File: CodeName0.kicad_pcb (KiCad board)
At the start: 4 copper layers, 60 x 80 mm, 96 parts, among them J1 STM32 Debug Conn, J2 Power Conn, J3 USB C 16p, J4 Telemetry Conn, J5 MicroSD, J6 GPS Conn, J7 Buzzer Conn, J8 ESP32 Jumper Conn, J9 ESP32 Programming Conn, Q1 MMBT3904, SW1 Tactile Switch, SW2 Tactile Switch, SW3 Tactile Switch, SW4 Tactile Switch, U1 TPS5430DDAR, U2 LDO, U3 STM32H743VITx, U4 ICM-42688-P, U5 BMP388, U6 ESP32 C3 WROOM 02U, Y1 Crystal_GND24

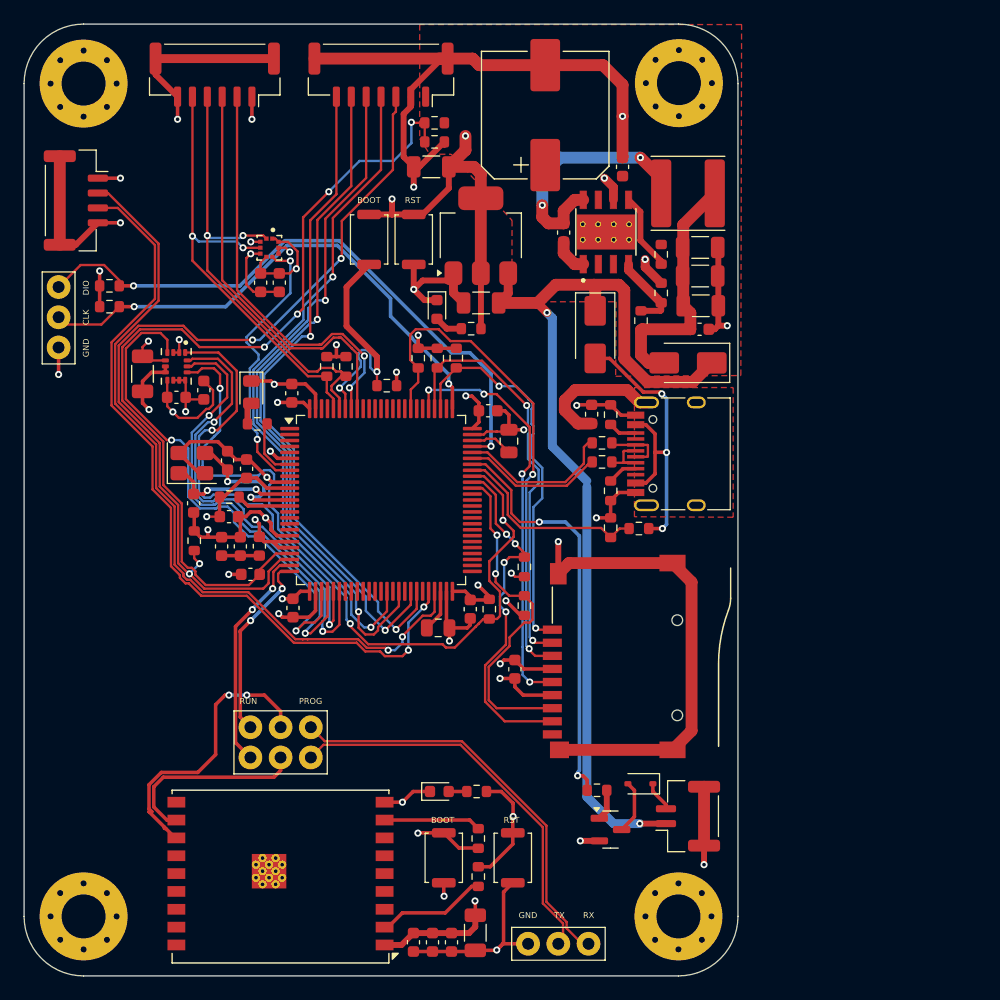
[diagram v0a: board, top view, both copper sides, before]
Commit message: feat: remove esp32-c3 wroom
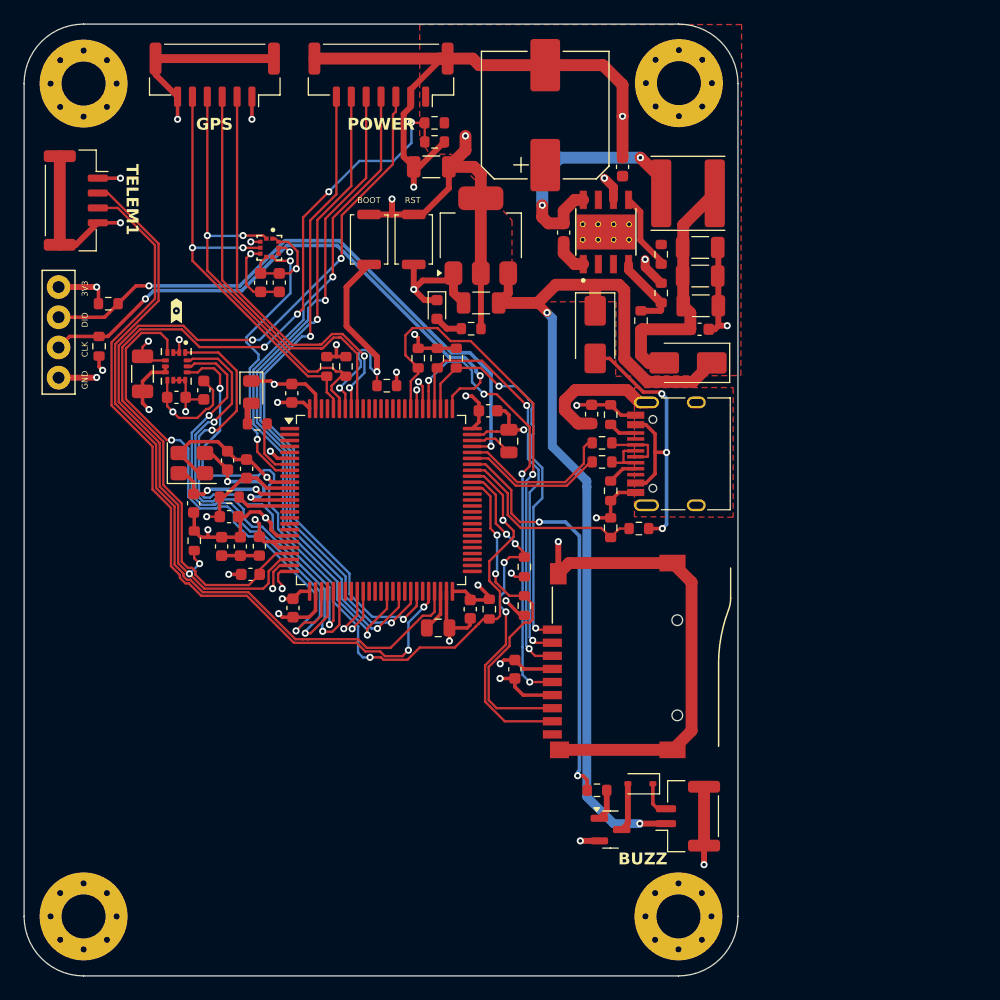
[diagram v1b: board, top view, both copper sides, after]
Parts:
- removed C24: 10uF, Capacitor_SMD:C_1206_3216Metric
- removed C25, C26, C28: 100nF, Capacitor_SMD:C_0603_1608Metric
- removed D4: LED, LED_SMD:LED_0603_1608Metric
- removed J8: ESP32 Jumper Conn, Connector_PinHeader_2.54mm:PinHeader_2x03_P2.54mm_Vertical
- removed J9: ESP32 Programming Conn, Connector_PinHeader_2.54mm:PinHeader_1x03_P2.54mm_Vertical
- removed R21: 330, Resistor_SMD:R_0603_1608Metric
- removed R29, R30: 10K, Resistor_SMD:R_0603_1608Metric
- removed SW3, SW4: Tactile Switch, Button_Switch_SMD:SW_Push_SPST_NO_Alps_SKRK
- removed U6: ESP32 C3 WROOM 02U, RF_Module:ESP32-C3-WROOM-02U
- added kibuzzard-68C3DDBA: G***, kibuzzard-68C3DDBA, F.Cu at (112.8, 84.1)
- J1: footprint Connector_PinHeader_2.54mm:PinHeader_1x03_P2.54mm_Vertical -> Connector_PinHeader_2.54mm:PinHeader_1x04_P2.54mm_Vertical
- moved R7 3.44 mm to (106.3, 87.1), turned to -90 degrees
- moved R6 1.50 mm to (107.1, 83.5)
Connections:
- J1 pad 1: SWDIO -> +3.3V
- J1 pad 2: SWCLK -> SWDIO
- J1 pad 3: GND -> SWCLK
- U3 pad 34: unconnected-(U3-PB0-Pad34) -> TIM3_CH3
- U3 pad 35: unconnected-(U3-PB1-Pad35) -> TIM3_CH4
- U3 pad 81: unconnected-(U3-PD0-Pad81) -> UART4_RX
- U3 pad 82: unconnected-(U3-PD1-Pad82) -> UART4_TX
- U3 pad 90: unconnected-(U3-PB4-Pad90) -> TIM3_CH1
- U3 pad 91: unconnected-(U3-PB5-Pad91) -> TIM3_CH2
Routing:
- net ESP_PROG_RX: track 34.9 -> 0.00 mm
- net ESP_PROG_TX: track 33.5 -> 0.00 mm
- net ESP32_TX: track 24.4 -> 0.00 mm, vias 2 -> 0
- net +3.3V: track 133.9 -> 111.1 mm, vias 23 -> 21
- net GND: track 267.0 -> 246.5 mm, vias 33 -> 30
- net ESP32_RX: track 16.4 -> 0.00 mm
- net USART2_TX: track 19.0 -> 3.03 mm, vias 2 -> 1
- net USART2_RX: track 15.9 -> 2.50 mm, vias 2 -> 1
- net Net-(U6-EN): track 9.29 -> 0.00 mm
- net Net-(U6-IO9): track 8.18 -> 0.00 mm
- net SWCLK: track 44.4 -> 48.4 mm
- net TIM3_CH3: track 0.00 -> 3.61 mm, vias 0 -> 1
- net TIM3_CH4: track 0.00 -> 3.54 mm, vias 0 -> 1
- net SDMMC_CLK: track 35.2 -> 38.2 mm
- net UART4_RX: track 0.00 -> 2.41 mm, vias 0 -> 1
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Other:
- board text added: "3V3"
- board text added: "BUZZ"
- board text added: "GPS"
- board text added: "POWER"
- board text added: "TELEM1"
- board text removed: "PROG"
- board text removed: "RUN"
- board text removed: "RX"
- board text removed: "TX"

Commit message: feat: ESP32-C3 schematic and pcb layout
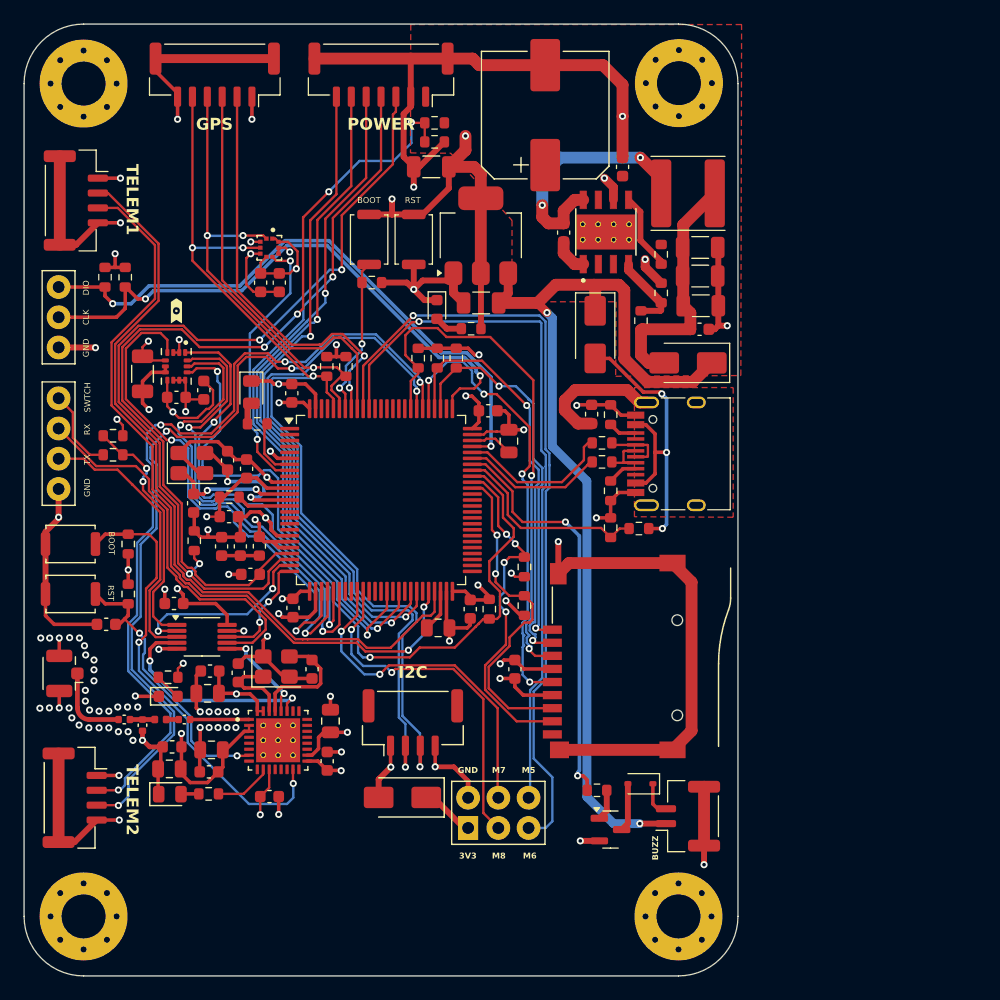
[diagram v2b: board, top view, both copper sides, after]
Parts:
- added C24: 1uF, Capacitor_SMD:C_0805_2012Metric, F.Cu at (115.4, 116.2)
- added C25: 1uF, Capacitor_SMD:C_0805_2012Metric, F.Cu at (115.8, 121.0)
- added C26: 10nF, Capacitor_SMD:C_0603_1608Metric, F.Cu at (115.6, 114.4)
- added C28: 100nF, Capacitor_SMD:C_0603_1608Metric, F.Cu at (125.5, 122.0)
- added C33: 10uF, Capacitor_SMD:C_0805_2012Metric, F.Cu at (112.2, 122.6)
- added C34: 100nF, Capacitor_SMD:C_0603_1608Metric, F.Cu at (120.6, 124.9)
- added C35: 100nF, Capacitor_SMD:C_0603_1608Metric, F.Cu at (115.5, 122.8)
- added C36: 1uF, Capacitor_SMD:C_0805_2012Metric, F.Cu at (125.8, 118.6)
- added C37: 100nF, Capacitor_SMD:C_0603_1608Metric, F.Cu at (106.9, 110.5)
- added C38: 1pF, Capacitor_SMD:C_0402_1005Metric, F.Cu at (108.4, 118.5)
- added C39: 100nF, Capacitor_SMD:C_0603_1608Metric, F.Cu at (112.6, 108.7)
- added C40: 15pF, Capacitor_SMD:C_0603_1608Metric, F.Cu at (118.0, 114.5)
- added C41: 15pF, Capacitor_SMD:C_0603_1608Metric, F.Cu at (124.2, 114.2)
- added C42: 1.5pF, Capacitor_SMD:C_0402_1005Metric, F.Cu at (110.0, 118.9)
- added C43: 100pF, Capacitor_SMD:C_0402_1005Metric, F.Cu at (113.5, 118.5)
- added D4: LED, LED_SMD:LED_0805_2012Metric, F.Cu at (112.2, 124.7)
- added D7: LED, LED_SMD:LED_0603_1608Metric, F.Cu at (112.1, 116.5)
- added D8: SS34, Diode_SMD:D_SMA, F.Cu at (131.8, 125.0)
- added FB3: FerriteBead, Inductor_SMD:L_0603_1608Metric, F.Cu at (112.4, 120.8)
- added J10: Telemetry 2 Conn, Connector_JST:JST_GH_SM04B-GHS-TB_1x04-1MP_P1.25mm_Horizontal, F.Cu at (104.2, 125.0)
- added J11: I2C, Connector_JST:JST_GH_BM04B-GHS-TBT_1x04-1MP_P1.25mm_Vertical, F.Cu at (132.7, 118.7)
- added J12: PWM Aux Conn, Connector_PinHeader_2.54mm:PinHeader_2x03_P2.54mm_Vertical, F.Cu at (142.4, 125.0)
- added J8: U.FL Hirose, Connector_Coaxial:U.FL_Hirose_U.FL-R-SMT-1_Vertical, F.Cu at (103.4, 114.6)
- added J9: ESP32 Prog Conn, Connector_PinHeader_2.54mm:PinHeader_1x04_P2.54mm_Vertical, F.Cu at (102.9, 91.5)
- added L2: 1.8nH, Inductor_SMD:L_0402_1005Metric, F.Cu at (111.5, 118.5)
- added R21: 10K, Resistor_SMD:R_0603_1608Metric, F.Cu at (108.8, 107.9)
- added R29: 10K, Resistor_SMD:R_0603_1608Metric, F.Cu at (108.8, 103.7)
- added R30: 10K, Resistor_SMD:R_0603_1608Metric, F.Cu at (107.5, 96.2)
- added R31: 10K, Resistor_SMD:R_0603_1608Metric, F.Cu at (107.5, 94.6)
- added R32: 330, Resistor_SMD:R_0603_1608Metric, F.Cu at (115.5, 124.7)
- added R33: 330, Resistor_SMD:R_0603_1608Metric, F.Cu at (112.1, 114.9)
- added SW3: Tactile Switch, Button_Switch_SMD:SW_Push_SPST_NO_Alps_SKRK, F.Cu at (103.9, 103.7)
- added SW4: Tactile Switch, Button_Switch_SMD:SW_Push_SPST_NO_Alps_SKRK, F.Cu at (103.9, 107.9)
- added U6: ESP32-C3FH4, ESP32-C3FH4:QFN50P500X500X90-33N, F.Cu at (121.3, 120.2)
- added U7: BCT4222CEAB-TR, Package_SO:MSOP-10_3x3mm_P0.5mm, F.Cu at (115.0, 111.5)
- added Y2: Crystal 40MHz, Crystal:Crystal_SMD_3225-4Pin_3.2x2.5mm, F.Cu at (121.2, 114.0)
- J1: footprint Connector_PinHeader_2.54mm:PinHeader_1x04_P2.54mm_Vertical -> Connector_PinHeader_2.54mm:PinHeader_1x03_P2.54mm_Vertical
- J4: value Telemetry Conn -> Telemetry 1 Conn
- R26, R27: value 4.7K -> 2.2K
- U2: value LDO -> AMS1117-3.3
- Y1: value Crystal_GND24 -> Crystal 25Mhz
- moved R25 8.76 mm to (129.2, 81.7)
- moved R7 6.20 mm to (108.5, 81.3), turned to 90 degrees
- moved R6 2.24 mm to (106.8, 81.3), turned to -90 degrees
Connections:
- J1 pad 1: +3.3V -> SWDIO
- J1 pad 2: SWDIO -> SWCLK
- J1 pad 3: SWCLK -> GND
- J2 pad MP: GND -> (no net)
- J4 pad MP: GND -> (no net)
- J6 pad MP: GND -> (no net)
- J7 pad MP: GND -> (no net)
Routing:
- net UART4_TX: track 1.58 -> 70.2 mm, vias 1 -> 4
- net UART4_RX: track 2.41 -> 70.3 mm, vias 1 -> 4
- net TIM3_CH2: track 0.00 -> 66.6 mm, vias 0 -> 1
- net GND: track 246.5 -> 311.8 mm, vias 30 -> 82
- net TIM3_CH1: track 0.00 -> 60.4 mm, vias 0 -> 1
- net I2C1_SCL: track 39.0 -> 85.1 mm, vias 2 -> 4
- net I2C1_SDA: track 37.8 -> 83.7 mm, vias 2 -> 4
- net +3.3V: track 111.1 -> 154.2 mm, vias 21 -> 30
- net ESP32_BOOT: track 0.00 -> 38.6 mm, vias 0 -> 2
- net ESP32_PROG_RX: track 0.00 -> 32.2 mm
- net TIM3_CH4: track 3.54 -> 30.0 mm, vias 1 -> 2
- net TIM3_CH3: track 3.61 -> 28.9 mm, vias 1 -> 2
- net ESP32_EN: track 0.00 -> 23.6 mm, vias 0 -> 2
- net ESP32_PROG_TX: track 0.00 -> 23.2 mm
- net Net-(U7-S): track 0.00 -> 20.7 mm, vias 0 -> 2
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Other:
- board text added: "I2C"
- board text added: "M5"
- board text added: "M6"
- board text added: "M7"
- board text added: "M8"
- board text added: "RX"
- board text added: "SWTCH"
- board text added: "TELEM2"
- board text added: "TX"

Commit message: feat: SX1280
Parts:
- added C44: 470nF, Capacitor_SMD:C_0603_1608Metric, F.Cu at (111.8, 135.2)
- added C45: 10nF, Capacitor_SMD:C_0603_1608Metric, F.Cu at (114.3, 132.1)
- added C46: 100nF, Capacitor_SMD:C_0603_1608Metric, F.Cu at (125.0, 129.8)
- added C47: 10uF, Capacitor_SMD:C_1206_3216Metric, F.Cu at (112.2, 128.2)
- added C48: 100nF, Capacitor_SMD:C_0603_1608Metric, F.Cu at (124.2, 132.3)
- added C49: 100nF, Capacitor_SMD:C_0603_1608Metric, F.Cu at (126.7, 128.5)
- added C50: 1nF, Capacitor_SMD:C_0603_1608Metric, F.Cu at (123.4, 129.8)
- added FB4: FerriteBead, Inductor_SMD:L_0603_1608Metric, F.Cu at (112.5, 120.3)
- added FB5: FerriteBead, Inductor_SMD:L_0603_1608Metric, F.Cu at (127.4, 125.2)
- added FB6: FerriteBead, Inductor_SMD:L_0603_1608Metric, F.Cu at (112.1, 126.2)
- added FB7: FerriteBead, Inductor_SMD:L_0603_1608Metric, F.Cu at (129.2, 130.5)
- added L3: 15uH, Inductor_SMD:L_Changjiang_FNR3015S, F.Cu at (111.6, 132.4)
- added R34: 10K, Resistor_SMD:R_0603_1608Metric, F.Cu at (131.6, 128.5)
- added U8: SX1280IMLTRT, SX1280IMLTRT:XCVR_SX1280IMLTRT, F.Cu at (118.9, 128.8)
- added Y3: OW7EL89CENUNFAYLC-52M, Crystal:Crystal_SMD_2016-4Pin_2.0x1.6mm, F.Cu at (129.2, 128.3)
- C24: value 1uF -> 10nF; footprint Capacitor_SMD:C_0805_2012Metric -> Capacitor_SMD:C_0603_1608Metric
- C25: value 1uF -> 100nF; footprint Capacitor_SMD:C_0805_2012Metric -> Capacitor_SMD:C_0603_1608Metric
- C26: value 10nF -> 1uF; footprint Capacitor_SMD:C_0603_1608Metric -> Capacitor_SMD:C_0805_2012Metric
- C33: value 10uF -> 1uF
- C34: value 100nF -> 1uF; footprint Capacitor_SMD:C_0603_1608Metric -> Capacitor_SMD:C_0805_2012Metric
- C36: value 1uF -> 10uF; footprint Capacitor_SMD:C_0805_2012Metric -> Capacitor_SMD:C_1206_3216Metric
- L1: footprint Inductor_SMD:L_Sunlord_SWPA6045S -> Inductor_SMD:L_Changjiang_FNR4020S
- Y1: value Crystal 25Mhz -> X322525MOB4SI
- Y2: value Crystal 40MHz -> X322540MPB4SI
- moved D7 15.5 mm to (126.6, 121.8), turned to 90 degrees
- moved R33 15.0 mm to (126.6, 118.6), turned to 90 degrees
- moved C28 9.98 mm to (115.6, 120.3), turned to 180 degrees
- moved C33 8.74 mm to (115.2, 114.4), turned to 0 degrees
- moved C34 8.74 mm to (112.3, 122.2)
- moved C36 7.33 mm to (124.7, 125.8)
- moved FB3 6.57 mm to (111.9, 114.2), turned to 0 degrees
- moved C26 4.33 mm to (111.7, 116.1)
- moved R2 3.27 mm to (153.6, 76.1)
- moved R3 3.27 mm to (153.6, 79.3)
- moved R5 2.97 mm to (153.6, 82.5)
- moved C4 2.90 mm to (156.8, 82.8)
- moved C8 2.90 mm to (156.8, 75.9)
- moved C5 2.90 mm to (156.9, 80.8)
- moved C6 2.90 mm to (156.8, 78.3)
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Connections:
- C24 pad 1: GND -> +3.3V
- C24 pad 2: +3.3V -> GND
- C26 pad 1: GND -> +3.3V
- C26 pad 2: +3.3V -> GND
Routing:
- net Net-(U8-DCC_FB): track 0.00 -> 31.2 mm, vias 0 -> 4
- net GND: track 311.8 -> 342.1 mm, vias 82 -> 89
- net +3.3V: track 154.2 -> 172.2 mm, vias 30 -> 34
- net ESP32_SCK: track 0.00 -> 15.8 mm, vias 0 -> 2
- net Net-(C50-Pad2): track 0.00 -> 15.6 mm
- net ESP32_MOSI: track 0.00 -> 15.0 mm, vias 0 -> 2
- net ESP32_MISO: track 0.00 -> 14.5 mm, vias 0 -> 2
- net ESP32_NSS: track 0.00 -> 13.9 mm, vias 0 -> 2
- net SX_RESET: track 0.00 -> 10.1 mm, vias 0 -> 2
- net Net-(U8-DCC_SW): track 0.00 -> 6.65 mm
- net SX_BUSY: track 0.00 -> 5.82 mm
- net SX_DIO1: track 0.00 -> 5.72 mm
- net +BATT: track 0.00 -> 4.28 mm
- net Net-(D1-A): track 21.3 -> 17.2 mm
- net Net-(U1-ENA): track 6.54 -> 3.87 mm
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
